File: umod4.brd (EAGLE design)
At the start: 104.9 x 69.8 mm, 72 parts, among them IC3 27C256-FEED-THRU, J1 DMSAT-SF-PEJ, J2 10118194-0001LF, J5 JST BM08B-SRSS, M1 RPi Pico W, M2 Generic single-sided NEO-8, Q1 C10487/SI2301CDS, Q2 SS8050, U1 74LVC541, U2 74LVC4245, U3 74LVC541, U4 RP2040, U5 W25Q128JVSIQ, U6 74LVC2G04, U7 74LVC2G04, U8 WS2812C-2020, Y1 12MHz

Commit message: All changes up to 4V1a fabrication
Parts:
- removed D2: Green, SparkFun-LED:LED-0603
- removed U8: WS2812C-2020, robins-v7:WS2812-2020
- added D3: C2761795/WS2812B, SparkFun-LED:WS2812B
- added LED1: KT-0805G, led:SML0805
- added LED2: KT-0805Y, led:SML0805
- added R9: 2.2K, SparkFun-03-01-2010:0402-RES
- J1: value DMSAT-SF-PEJ -> (none); device robins:DM3AT -> robins-v7:DM3AT
- J3: value JST BM08B-SRSS -> (none)
- moved TP2 12.4 mm to (90.9, 3.05)
- moved R13 6.51 mm to (60.5, 40.6)
- moved JP2 3.30 mm to (51.1, 35.6), turned to 90 degrees
- moved C26 3.06 mm to (26.4, 4.57)
- moved C14 1.63 mm to (22.9, 35.8), turned to 90 degrees
- moved TP1 1.52 mm to (101.9, 45.2)
- moved C27 1.44 mm to (24.9, 35.8), turned to 90 degrees
- moved R3 1.27 mm to (49.5, 30.0), turned to 0 degrees
- moved R14 1.02 mm to (23.9, 29.7)
- moved R15 1.02 mm to (23.9, 32.0)
- moved R5 0.51 mm to (39.4, 4.32)
- moved C21 0.25 mm to (91.7, 49.8)
- moved R11 0.25 mm to (90.2, 50.8)
- moved J1 0.16 mm to (18.3, 35.3)
- renumbered J5 to J3
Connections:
- removed net N$21: J1.DAT2, R15.1
- removed net N$22: J1.DAT1, R16.1
- removed net SPARE3: M1.20
- removed net SPARE4: M1.7
- removed net WS2812_DO: U8.1
- new net DAT1: J1.8, M1.17, R16.1
- new net DAT2: J1.1, M1.19, R15.1
- new net N$3: LED2.A, R9.2
- net !CARD: now also J1.B, M1.9; no longer J1.CARD_B, M1.19
- net +3V3: now also J1.4; no longer J1.VDD
- net +5_ECU: now also R9.1
- net DBG_BSY: now also LED1.C; no longer D2.C
- net GND: now also D3.3, J1.6, J1.A, LED2.C; no longer J1.CARD_A, J1.VSS, U8.2
- net N$6: now also LED1.A; no longer D2.A
- net SPARE2: now also M1.7; no longer M1.9
- net SPI1_CS: now also J1.2, M1.20; no longer J1.CD/DAT3, M1.17
- net SPI1_MISO: now also J1.7; no longer J1.DAT0
- net SPI1_MOSI: now also J1.3; no longer J1.CMD
- net SPI1_SCK: now also J1.5; no longer J1.CLK
- net VSYS: now also D3.1; no longer U8.4
- net WS2812_DI: now also D3.4; no longer U8.3
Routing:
- net DAT1: track 0.00 -> 36.6 mm
- net !CARD: track 18.5 -> 36.8 mm, vias 0 -> 1
- net PICOW_U1_RX: track 47.6 -> 62.1 mm
- net DAT2: track 0.00 -> 12.3 mm
- net PICOW_U1_TX: track 54.7 -> 66.7 mm
- net GPS_PPS: track 53.3 -> 63.0 mm
- net SPI1_MOSI: track 20.4 -> 29.4 mm
- net +3V3: track 329.3 -> 337.7 mm
- net SPI1_MISO: track 25.7 -> 32.4 mm
- net N$14: track 2.49 -> 8.51 mm
- net VSYS: track 49.9 -> 55.4 mm
- net N$21: track 4.62 -> 0.00 mm
- net SPARE3: track 4.34 -> 0.00 mm, vias 1 -> 0
- net N$22: track 4.24 -> 0.00 mm
- net SPARE4: track 3.56 -> 0.00 mm, vias 1 -> 0
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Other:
- board text added: "UltraMod 4V1a"
- board text added: "github.com/mookiedog/umod4-PCB"
- board text removed: "SP3"
- board text removed: "SP4"
- board text removed: "UltraMod 4V1"

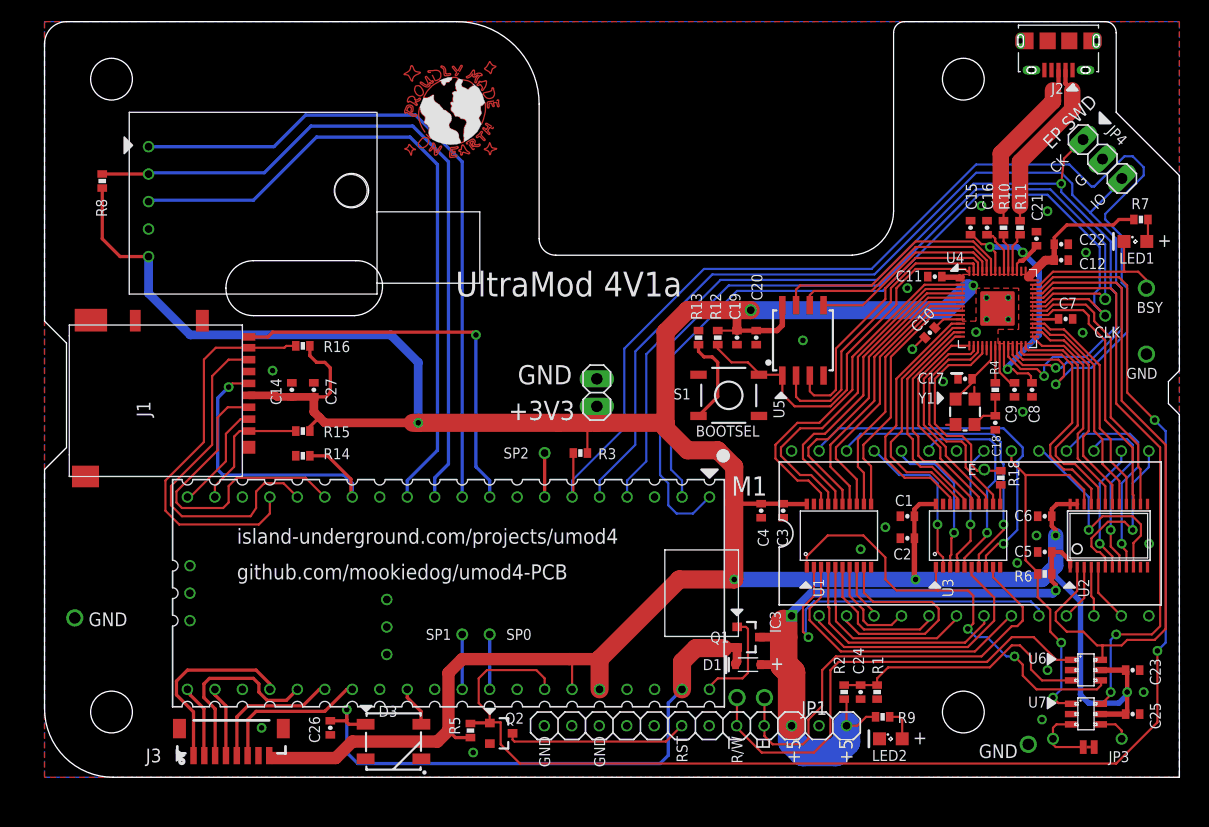
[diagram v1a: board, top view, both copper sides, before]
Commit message: Updates for 4V2 work-in-progress
- Latest version of 4V2 incorporating changes as per Changelist-4V2.md
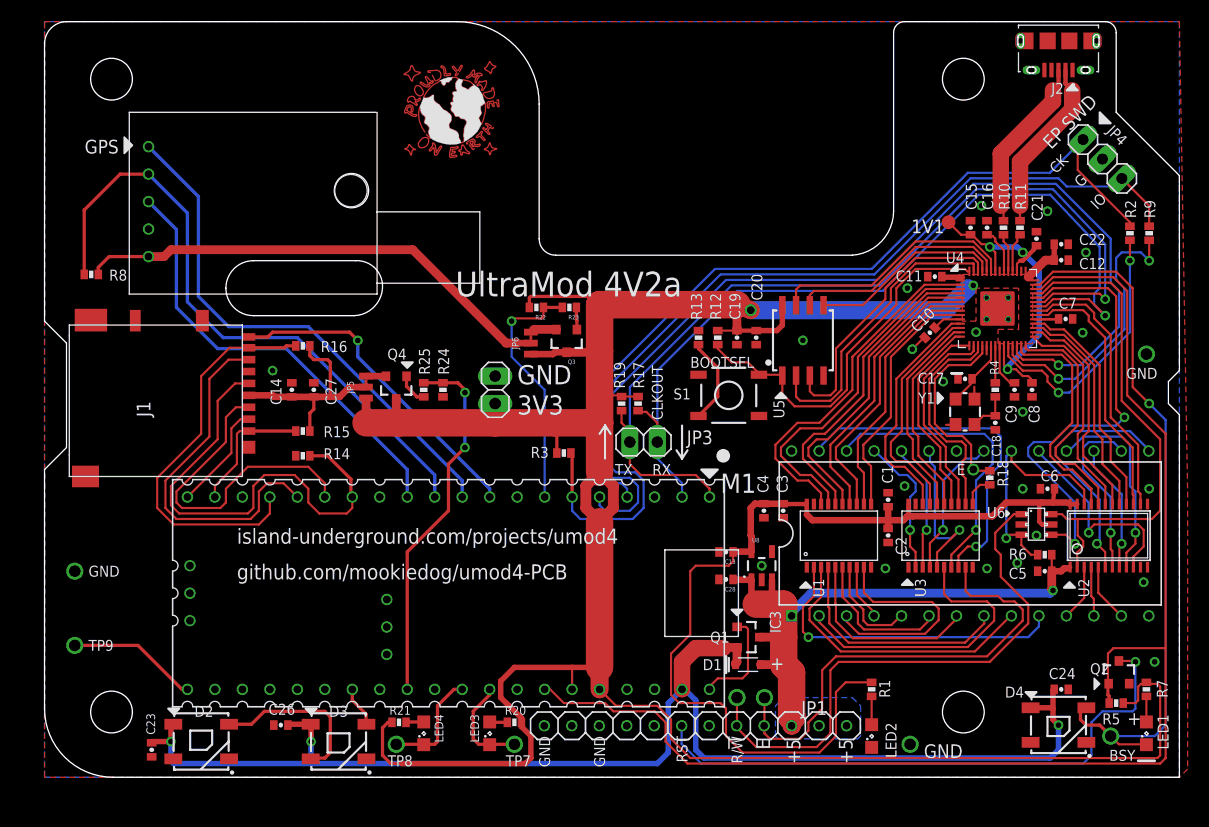
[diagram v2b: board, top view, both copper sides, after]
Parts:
- removed C25: 100n/16V/X7R, SparkFun-03-01-2010:0402-CAP
- removed J3: (no value), robins-v7:JST-SH-1.0MM-8V
- removed U7: 74LVC2G04, robins-v7:SOT23-6
- added 1V1: TPB1,27, testpad:B1,27
- added C13, C28: 1u/25V/X5R, SparkFun-03-01-2010:0402-CAP
- added D2, D4: C2761795/WS2812B, SparkFun-LED:WS2812B
- added JP5, JP6: JUMPER-SMT_3_1-NC_TRACE_NO-SILK, SparkFun-Jumpers:SMT-JUMPER_3_1-NC_TRACE_NO-SILK
- added LED3, LED4: KT-0805G, led:SML0805
- added Q3, Q4: C10487/SI2301CDS, robins-v7:SOT23
- added R17, R19, R22, R24: 10K, SparkFun-03-01-2010:0402-RES
- added R20, R21: 470R, SparkFun-03-01-2010:0402-RES
- added R23, R25: 1K, SparkFun-03-01-2010:0402-RES
- added TP7, TP8, TP9: (no value), robins-v7:KEYSTONE-1035
- added U8: 3.3V/150mA, SparkFun-IC-Power:SOT23-5
- JP3: value NC -> (none); device SparkFun-Jumpers:SMT-JUMPER_2_NC_TRACE_NO-SILK -> pinhead:1X02
- R1: value 10K -> 1K
- R2: value 5K1 -> 100R
- R9: value 2.2K -> 100R
- moved C23 91.0 mm to (9.91, 2.54), turned to 270 degrees
- moved R5 59.7 mm to (99.1, 6.86), turned to 0 degrees
- moved Q2 57.4 mm to (99.3, 9.65), turned to 0 degrees
- moved R9 51.0 mm to (102.1, 50.3), turned to 90 degrees
- moved R2 50.0 mm to (100.3, 50.3)
- moved JP3 49.9 mm to (55.4, 31.0)
- moved LED1 45.5 mm to (101.9, 4.06), turned to 90 degrees
- moved R7 43.4 mm to (101.9, 8.13), turned to 270 degrees
- moved TP1 41.5 mm to (98.6, 3.81)
- moved C24 18.5 mm to (94.0, 8.13), turned to 0 degrees
- moved U6 14.2 mm to (91.7, 23.4)
- moved TP2 10.9 mm to (80.0, 3.05)
- moved JP2 9.40 mm to (41.7, 35.8)
- moved R8 8.70 mm to (4.32, 46.5), turned to 0 degrees
- moved D3 5.08 mm to (27.2, 3.30)
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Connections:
- removed net !ECU_PWR!: U1.1, U3.1, U6.4
- removed net LCD_BKLT: J3.6, M1.27
- removed net LCD_DC: J3.5, M1.26
- removed net NC1_IN: JP3.2, U7.3
- removed net NC1_OUT: U7.4
- removed net SPI0_CS: J3.4, M1.22
- removed net SPI0_MISO: J3.2, M1.21
- removed net SPI0_MOSI: J3.3, M1.25
- removed net SPI0_SCK: J3.1, M1.24
- new net 3V3_GPS_EN: M1.7, R22.1, R23.2
- new net 3V3_SD_EN: M1.29, R24.2, R25.1
- new net 3V3_SD_SW: JP5.3, Q4.S
- new net 3V3_SW: JP6.3, Q3.S
- new net N$16: R9.1, U4.25
- new net N$19: D2.4, D3.2
- new net N$21: LED3.A, R20.2
- new net N$22: LED4.A, R21.2
- new net N$23: Q4.G, R25.2
- new net N$25: Q3.G, R23.1
- new net VCCB: C1.1, C13.1, C2.1, C3.1, C4.1, C6.1, R1.1, U1.20, U2.23, U2.24, U3.20, U6.5, U8.5
- new net VCC_GPS: JP6.2, M2.5, R8.2
- new net VDD_SD: C14.1, C27.1, J1.4, JP5.2, R15.2, R16.2
- net !CE!_5V: now also U6.3; no longer U7.1
- net +3V3: now also JP5.1, JP6.1, Q3.D, Q4.D, R17.1, R19.1, R20.1, R21.1, R22.2; no longer C1.1, C14.1, C2.1, C23.1, C25.1, C27.1, C3.1, C4.1, C6.1, J1.4, J3.8, M2.5, R15.2, R16.2, R8.2, U1.20, U2.23, U2.24, U3.20, U6.5, U7.5
- net +5_ECU: now also C28.1, U8.1, U8.3; no longer R2.1, R9.1
- net 1.0V: now also 1V1.TP
- net CE: now also U6.4; no longer U7.6
- net DBG_BSY: now also D4.4
- net GND: now also C13.2, C28.2, D2.3, D4.3, R24.1, U1.1, U3.1, U8.2; no longer C25.2, J3.7, JP3.1, R1.2, U7.2
- net N$3: now also R1.2; no longer R9.2
- net N$4: now also R2.1, U4.24; no longer C24.1, R1.1, R2.2, U6.3
- net PICOW_U0_RX: now also JP3.1, R17.2
- net PICOW_U0_TX: now also JP3.2, R19.2
- net RP_SWCLK: now also R2.2; no longer U4.24
- net RP_SWD: now also R9.2; no longer U4.25
- net SPARE0: now also LED3.C, TP7.P$1
- net SPARE1: now also LED4.C, TP8.P$1
- net SPARE2: now also M1.21, TP9.P$1; no longer M1.7
- net VSYS: now also C23.1, C24.1, D2.1, D4.1
- net WS2812_DI: now also M1.27; no longer M1.29
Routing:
- net VCCB: track 0.00 -> 91.2 mm
- net +3V3: track 337.7 -> 262.5 mm, vias 7 -> 2
- net VSYS: track 55.4 -> 123.2 mm, vias 1 -> 3
- net DBG_BSY: track 14.7 -> 66.0 mm, vias 0 -> 1
- net VCC_GPS: track 0.00 -> 44.9 mm
- net !ECU_PWR!: track 42.0 -> 0.00 mm, vias 2 -> 0
- net !RESET!_5V: track 16.9 -> 54.1 mm, vias 0 -> 1
- net 3V3_SD_EN: track 0.00 -> 34.0 mm, vias 0 -> 2
- net N$16: track 0.00 -> 26.4 mm, vias 0 -> 2
- net 3V3_GPS_EN: track 0.00 -> 23.2 mm, vias 0 -> 1
- net PICOW_U1_RX: track 62.1 -> 40.9 mm
- net VDD_SD: track 0.00 -> 20.8 mm
- net SPI0_SCK: track 17.6 -> 0.00 mm
- net SPI0_MOSI: track 17.6 -> 0.00 mm
- net RP_SWCLK: track 93.2 -> 76.8 mm, vias 2 -> 0
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- added copper zone on layer 16, net +5_ECU
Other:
- board text added: "3V3"
- board text added: "CLKOUT"
- board text added: "GPS"
- board text added: "RX"
- board text added: "TX"
- board text added: "UltraMod 4V2a"
- board text removed: "+3V3"
- board text removed: "CLK"
- board text removed: "SP0"
- board text removed: "SP1"
- board text removed: "SP2"
- board text removed: "UltraMod 4V1a"
